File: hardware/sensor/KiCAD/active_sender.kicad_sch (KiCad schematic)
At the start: 32 parts, among them J1 Conn_01x04_Pin, J2 USB-C connector, J3 Water Sensor, Q1 AO3400A, Q2 AO3401A, Q3 AO3401A, SW1 SW_Push, SW2 SW_SPDT, U1 HT7750_C250900, U3 AMS1117-3.3, U4 E77-900M22S

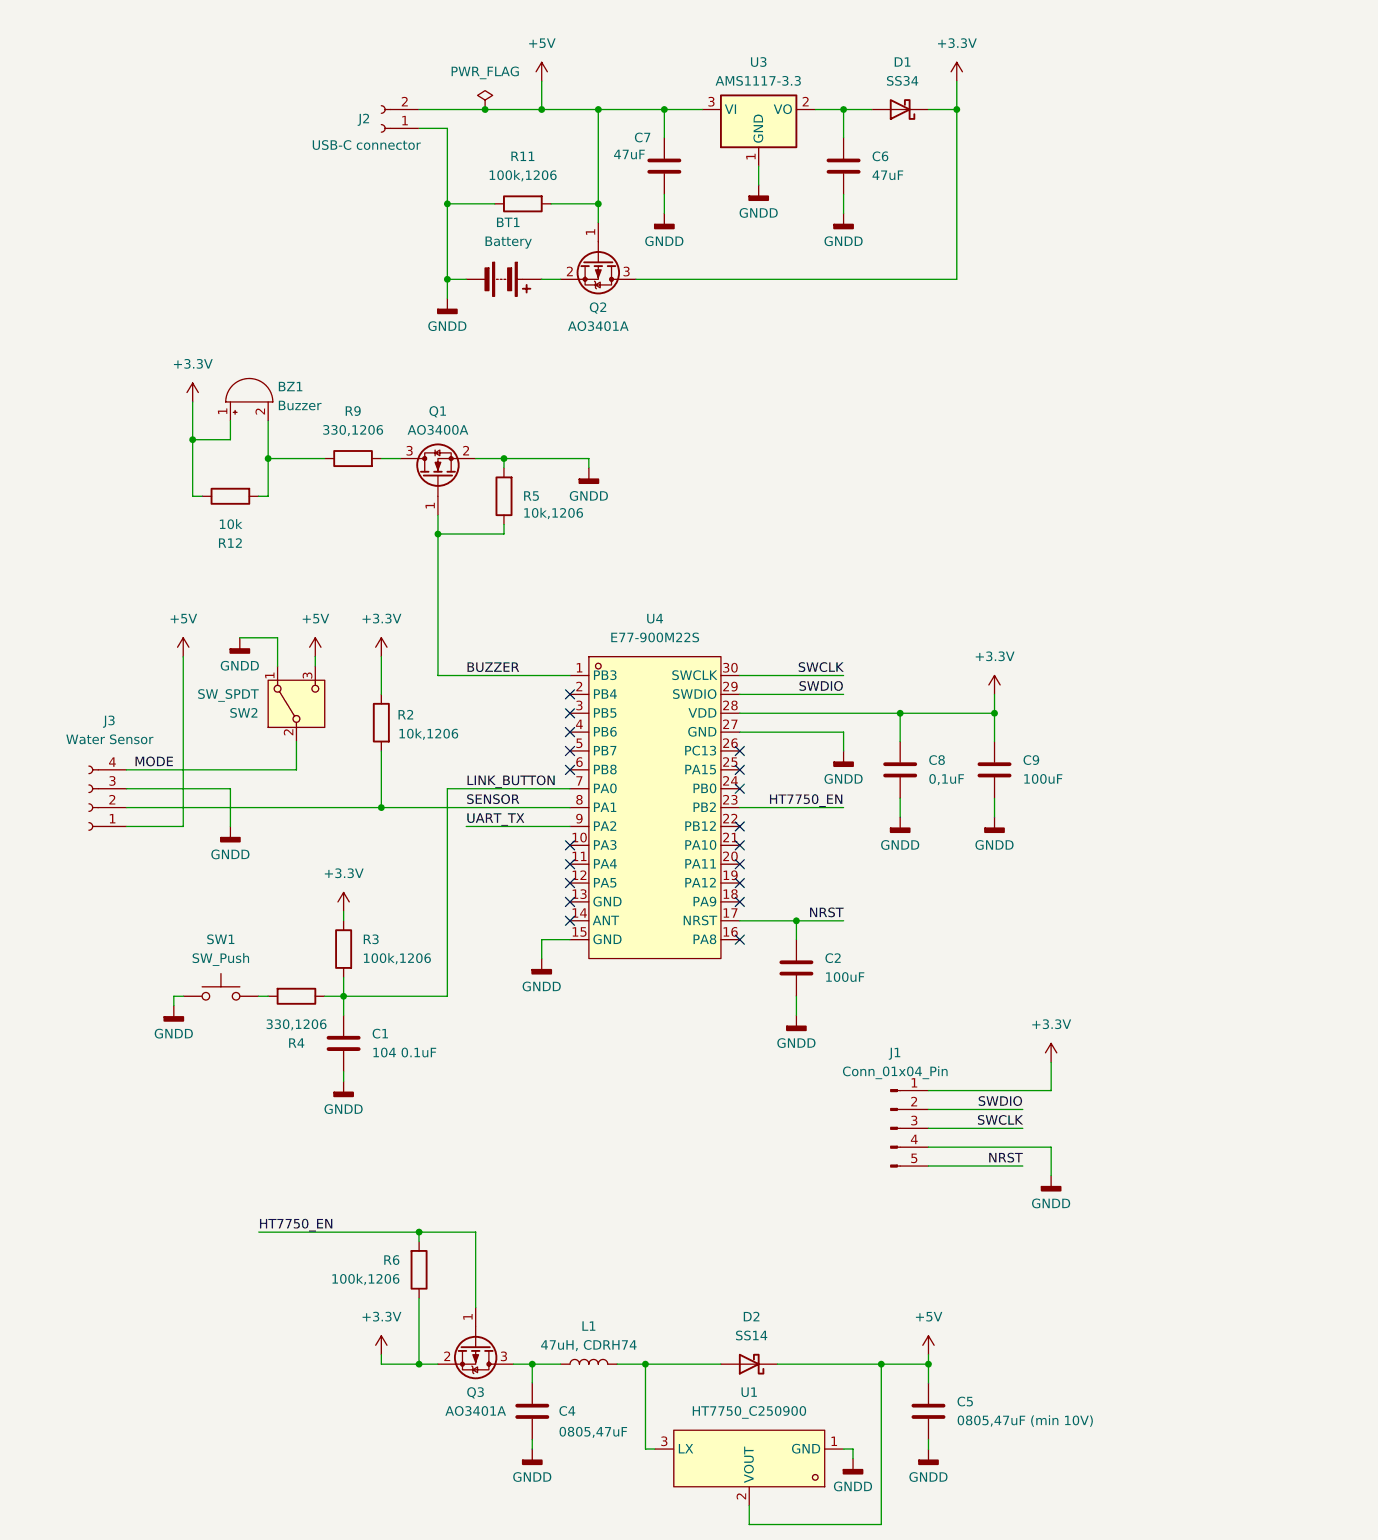
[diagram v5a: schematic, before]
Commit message: added alarm acknowledge and many code improvements
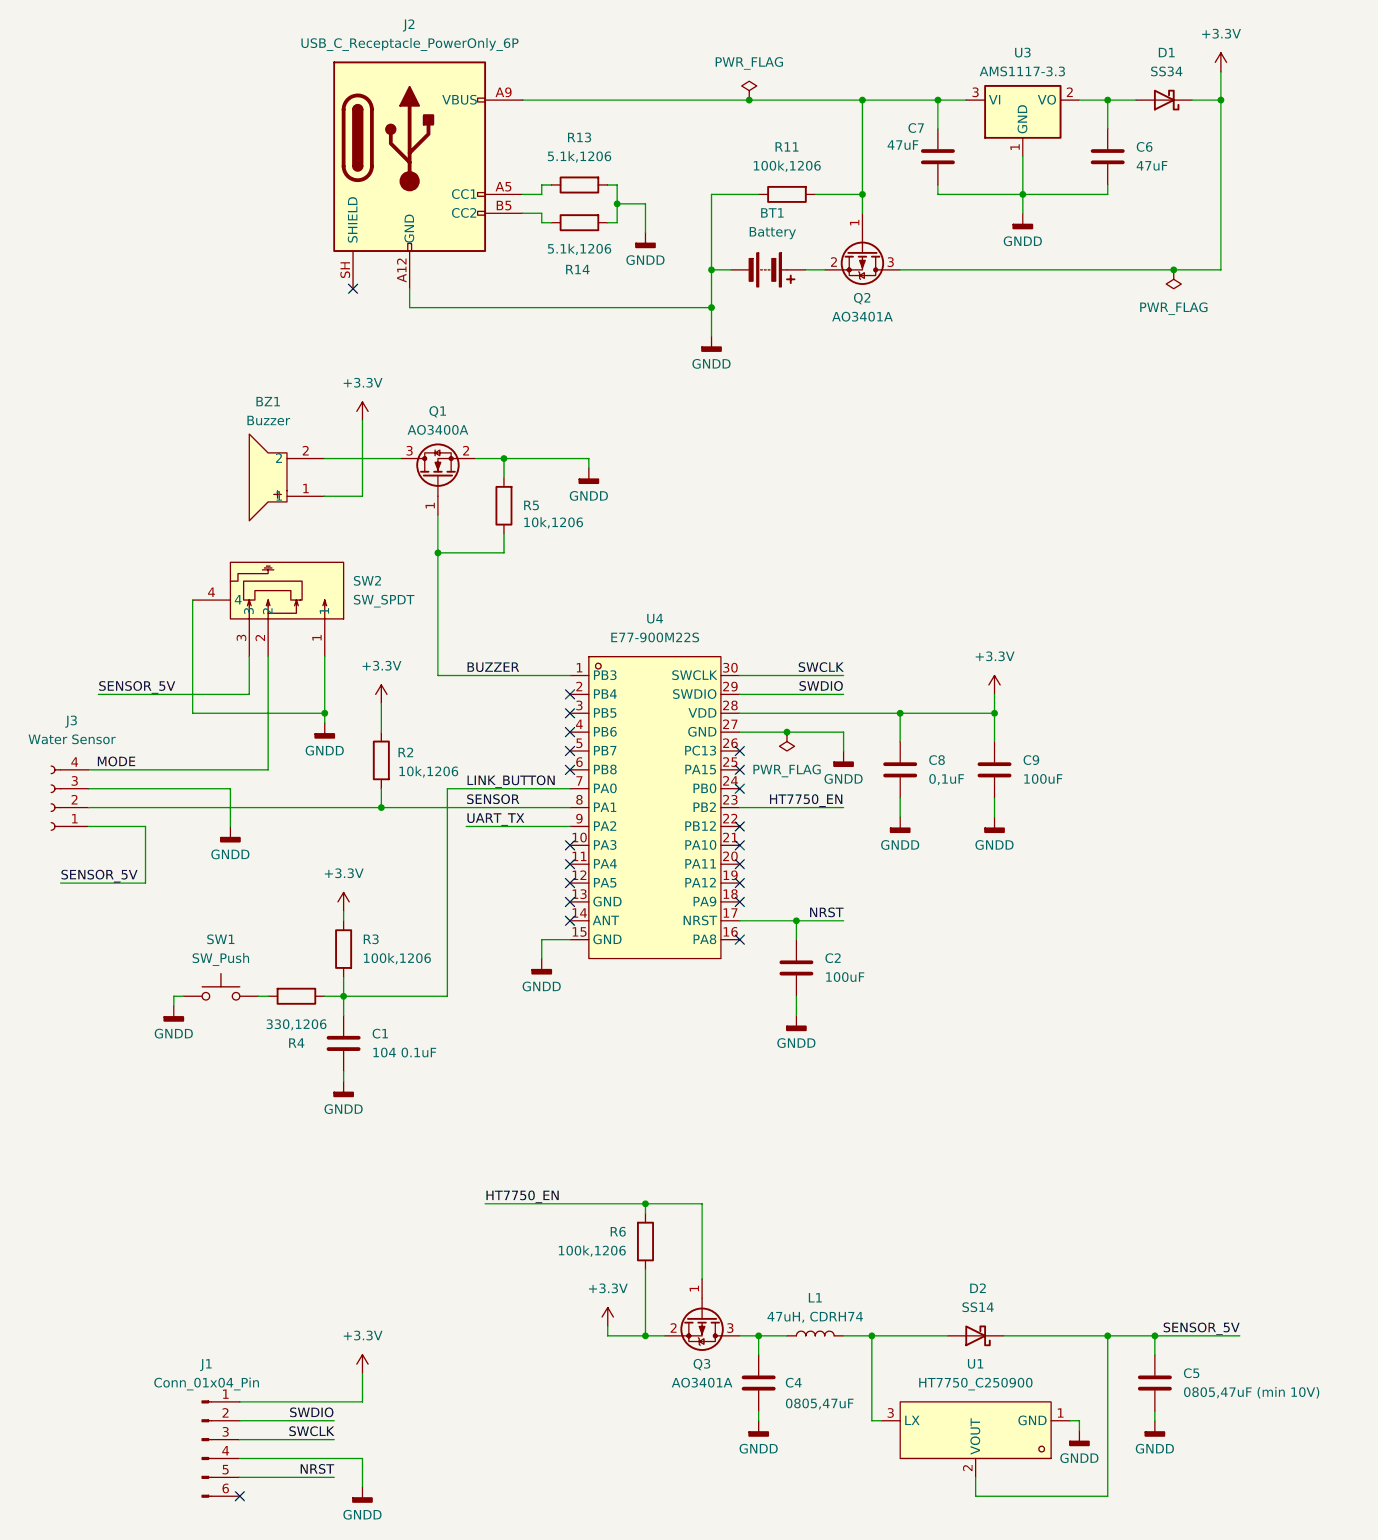
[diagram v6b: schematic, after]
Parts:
- removed J2: USB-C connector, Connector_JST:JST_PH_B2B-PH-K_1x02_P2.00mm_Vertical, symbol Connector:Conn_01x02_Socket
- removed R12: 10k, Resistor_SMD:R_1206_3216Metric_Pad1.30x1.75mm_HandSolder, symbol Device:R
- removed R9: 330,1206, Resistor_SMD:R_1206_3216Metric_Pad1.30x1.75mm_HandSolder, symbol Device:R
- added J2: USB_C_Receptacle_PowerOnly_6P, Connector_USB:USB_C_Receptacle_GCT_USB4125-xx-x-0190_6P_TopMnt_Horizontal, symbol Connector:USB_C_Receptacle_PowerOnly_6P
- added R13, R14: 5.1k,1206, Resistor_SMD:R_1206_3216Metric_Pad1.30x1.75mm_HandSolder, symbol Device:R
- BT1: footprint custom_footprints:BHC-CR123A -> custom_footprints:CR123A-SMD_BH-123A-B5BA003
- BZ1: footprint Buzzer_Beeper:Buzzer_12x9.5RM7.6 -> custom_footprints:Huaneng MLT-9650; symbol Device:Buzzer -> Custom_library:HND-9650B; LCSC Part (none) -> C96127; MPN (none) -> MLT-9650; Manufacturer (none) -> 华能
- J1: footprint Connector_PinHeader_2.00mm:PinHeader_1x05_P2.00mm_Vertical -> Connector_PinHeader_2.54mm:PinHeader_2x03_P2.54mm_Vertical_SMD; symbol Connector:Conn_01x05_Pin -> Connector:Conn_01x06_Pin
- J3: footprint Connector_JST:JST_XH_S4B-XH-A-1_1x04_P2.50mm_Horizontal -> Connector_JST:JST_XH_S4B-XH-SM4-TB_1x04-1MP_P2.50mm_Horizontal
- SW1: footprint Button_Switch_THT:SW_PUSH_6mm_H5mm -> Button_Switch_SMD:SW_Push_1TS009xxxx-xxxx-xxxx_6x6x5mm
- SW2: footprint custom_footprints:SS12D00 -> custom_footprints:MSK12-C02; symbol Switch:SW_SPDT -> Custom_library:MSK12C02; LCSC Part (none) -> C431540; MPN (none) -> MSK12C02; Manufacturer (none) -> SHOU HAN(首韩)
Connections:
- net GNDD: now also SW2.4, J2.A12 (GND), J2.B12 (GND), R13.2, R14.2
- net at BZ1.2: now also Q1.3 (D)
- net +5V renamed SENSOR_5V
- net SENSOR_5V: no longer C7.1, Q2.1 (G), R11.2, U3.3 (VI)
- new net: J2.A5 (CC1), R13.1
- new net: C7.1, J2.A9 (VBUS), J2.B9 (VBUS), Q2.1 (G), R11.2, U3.3 (VI)
- new net: J2.B5 (CC2), R14.1
- no-connect marks 19 -> 21
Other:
- moved on the sheet: BT1, C4, C5, C6, C7, D1, D2, J3, L1, Q2, Q3, R11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
